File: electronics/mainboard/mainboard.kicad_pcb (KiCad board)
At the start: 2 copper layers, 43 x 137 mm, 20 parts, among them Q1 DMN2020LSN-7, SW1 SW_Push, SW10 SW_Push, SW11 SW_Push, SW12 SW_Push, SW13 SW_Push, SW14 SW_Push, SW15 SW_Push, SW2 SW_Push, SW3 SW_Push, SW4 SW_Push, SW5 SW_Push, SW6 SW_Push, SW7 SW_Push, SW8 SW_Push, SW9 SW_Push, U1 1022

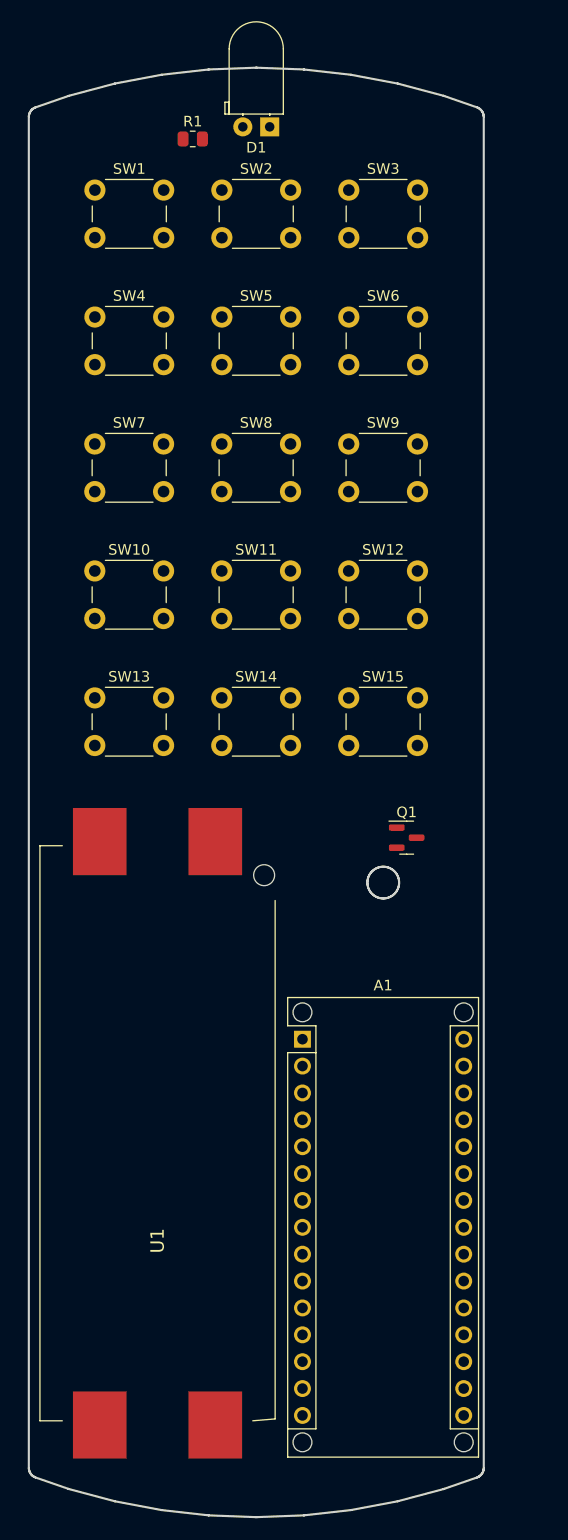
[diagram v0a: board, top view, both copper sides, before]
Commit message: modify closing mechanism and printing improvements - remove rounding (minkowski) for better printability - add closing mechanisms with levers   => remove backring as no longer needed   => remove positioning slits - correct case height to fit pcb - regenerate pcb outline and pcb 3d model because of some of the above changes
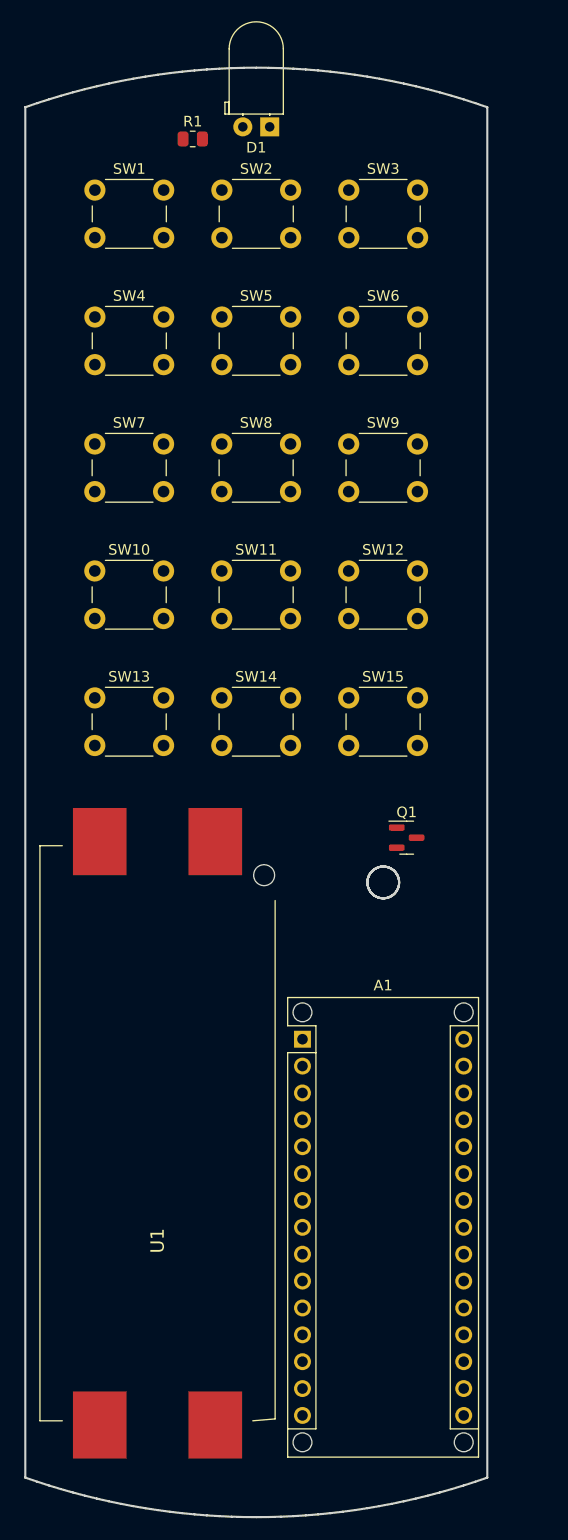
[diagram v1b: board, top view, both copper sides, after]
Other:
- board size 43 x 137 mm -> 43.7 x 137 mm

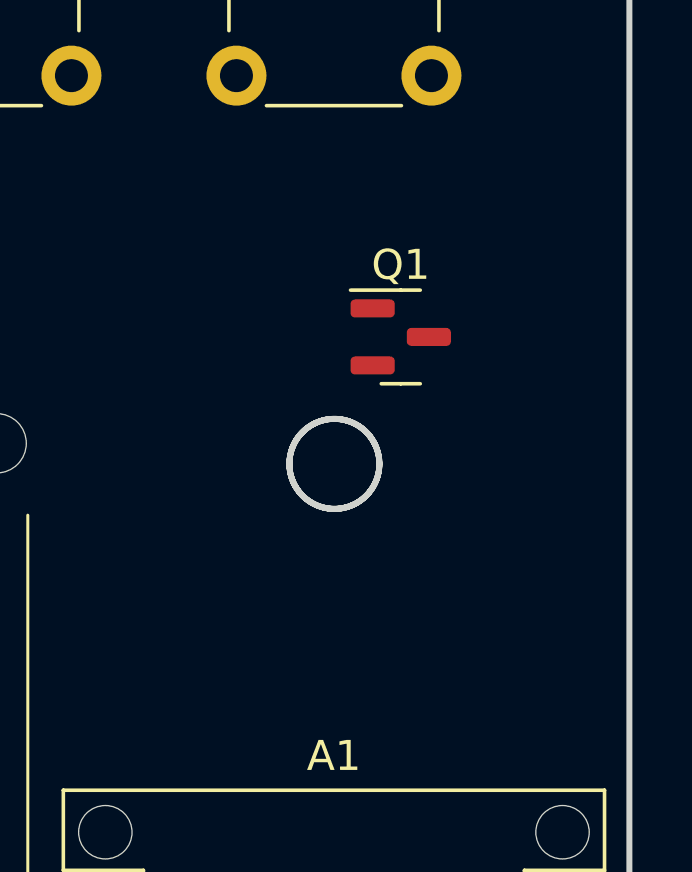
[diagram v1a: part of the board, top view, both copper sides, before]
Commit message: clean up libraries and  add more parts to desing - clean up libraries folder structure - no longer ignore important library table files - ignore auto save files - add fet for polarity protection - add buffer capacitors
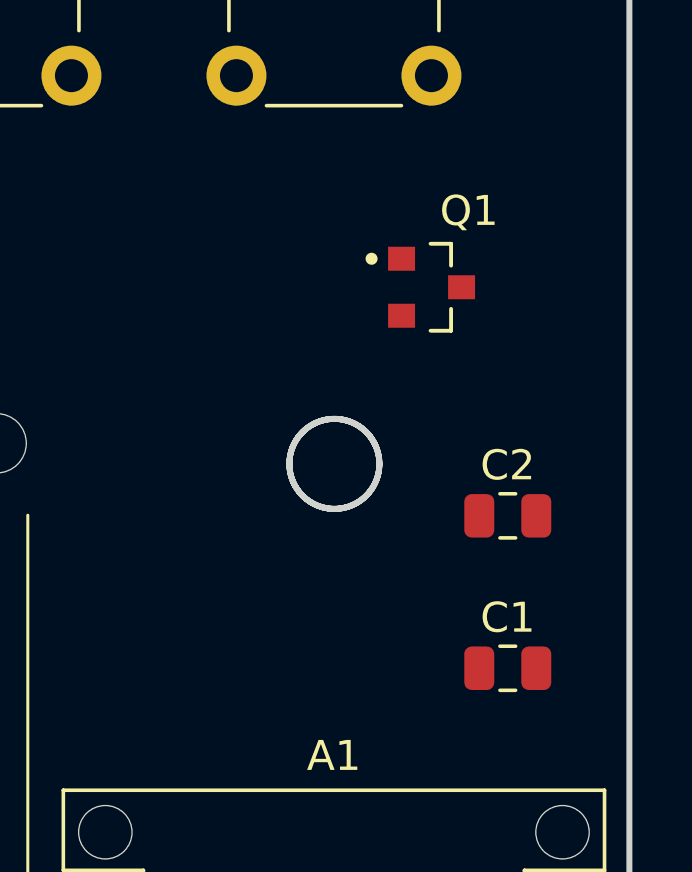
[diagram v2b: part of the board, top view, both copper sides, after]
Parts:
- added C1: 100u, Capacitor_SMD:C_0805_2012Metric, F.Cu at (128.0, 127.9)
- added C2: 100n, Capacitor_SMD:C_0805_2012Metric, F.Cu at (128.0, 122.8)
- Q1: value DMN2020LSN-7 -> TSM250N02CX_RFG; footprint Package_TO_SOT_SMD:SOT-23 -> TSM250N02CX_RFG:TRANS_TSM250N02CX_RFG
- moved Q1 1.95 mm to (125.5, 115.2)

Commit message: driver for ir-led and minor optimizations
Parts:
- added JP1: SolderJumper_2_Bridged, Jumper:SolderJumper-2_P1.3mm_Bridged_Pad1.0x1.5mm, F.Cu at (90.9, 110.1)
- added Q2: TSM250N02CX_RFG, TSM250N02CX_RFG:TRANS_TSM250N02CX_RFG, F.Cu at (120.4, 49.1)
- D1: value LED -> IR333-A
- R1: value R -> 82 1% 35mW
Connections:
- D1 pad 1: GND -> Net-(D1-Pad1)
- R1 pad 1: Net-(A1-Pad19) -> Net-(D1-Pad2)
- R1 pad 2: Net-(D1-Pad2) -> +3V0
- U1 pad 2: +3V0 -> Net-(U1-Pad2)
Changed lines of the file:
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@@
   (net 31 "Net-(A1-Pad19)")
   (net 32 "Net-(Q1-Pad3)")
+  (net 33 "Net-(D1-Pad1)")
+  (net 34 "Net-(U1-Pad2)")
+  (footprint "TSM250N02CX_RFG:TRANS_TSM250N02CX_RFG" (layer "F.Cu")
+    (at 120.4071 49.1437)
+    (property "MANUFACTURER" "Taiwan Semiconductor")
+    (property "MAXIMUM_PACKAGE_HEIGHT" "1.15mm")
+    (property "PARTREV" "A2007")
+    (property "STANDARD" "Manufacturer Recommendation")
+    (property "Sheetfile" "mainboard.kicad_sch")
+    (property "Sheetname" "")
+    (attr through_hole)
+    (fp_text reference "Q2" (at 1.25 -3.135) (layer "F.SilkS")
+      (effects (font (size 1 1) (thickness 0.15)))
+    )
+    (fp_text value "TSM250N02CX_RFG" (at 11.41 3.135) (layer "F.Fab")
+      (effects (font (size 1 1) (thickness 0.15)))
+    )
+    (fp_line (start -0.035 1.45) (end 0.65 1.45) (layer "F.SilkS") (width 0.127))
+    (fp_line (start 0.65 -1.45) (end -0.035 -1.45) (layer "F.SilkS") (width 0.127))
+    (fp_line (start 0.65 1.45) (end 0.65 0.72) (layer "F.SilkS") (width 0.127))
+    (fp_line (start 0.65 -0.72) (end 0.65 -1.45) (layer "F.SilkS") (width 0.127))
+    (fp_circle (center -2 -0.95) (end -1.9 -0.95) (layer "F.SilkS") (width 0.2) (fill none))
+    (fp_line (start -1.7 1.7) (end 1.7 1.7) (layer "F.CrtYd") (width 0.05))
+    (fp_line (start -1.7 -1.7) (end -1.7 1.7) (layer "F.CrtYd") (width 0.05))
+    (fp_line (start 1.7 1.7) (end 1.7 -1.7) (layer "F.CrtYd") (width 0.05))
+    (fp_line (start 1.7 -1.7) (end -1.7 -1.7) (layer "F.CrtYd") (width 0.05))
+    (fp_line (start -0.65 -1.45) (end -0.65 1.45) (layer "F.Fab") (width 0.127))
+    (fp_line (start -0.65 1.45) (end 0.65 1.45) (layer "F.Fab") (width 0.127))
+    (fp_line (start 0.65 -1.45) (end -0.65 -1.45) (layer "F.Fab") (width 0.127))
+    (fp_line (start 0.65 1.45) (end 0.65 -1.45) (layer "F.Fab") (width 0.127))
+    (fp_circle (center -2 -0.95) (end -1.9 -0.95) (layer "F.Fab") (width 0.2) (fill none))
+    (pad "1" smd rect locked (at -1 -0.95) (size 0.9 0.8) (layers "F.Cu" "F.Paste" "F.Mask")
+      (net 31 "Net-(A1-Pad19)") (pintype "passive"))
+    (pad "2" smd rect locked (at -1 0.95) (size 0.9 0.8) (layers "F.Cu" "F.Paste" "F.Mask")
+      (net 16 "GND") (pintype "passive"))
+    (pad "3" smd rect locked (at 1 0) (size 0.9 0.8) (layers "F.Cu" "F.Paste" "F.Mask")
+      (net 33 "Net-(D1-Pad1)") (pintype "passive"))
+    (model "${KIPRJMOD}/lib/TSM250N02CX_RFG/TSM250N02CX_RFG.step"
+      (offset (xyz 0 0 0))
+      (scale (xyz 1 1 1))
+      (rotate (xyz -90 0 0))
+    )
+  )
   (footprint "Capacitor_SMD:C_0805_2012Metric" (layer "F.Cu")
     (at 128.0271 122.8037)
@@
     (property "Sheetfile" "mainboard.kicad_sch")
     (property "Sheetname" "")
-    (property "exclude_from_bom" "")
-    (attr smd exclude_from_bom)
+    (attr smd)
     (fp_text reference "C2" (at 0 -1.68) (layer "F.SilkS")
       (effects (font (size 1 1) (thickness 0.15)))
@@
       (effects (font (size 1 1) (thickness 0.15)))
     )
-    (fp_text value "R" (at 0 1.65) (layer "F.Fab")
+    (fp_text value "82 1% 35mW" (at 0 1.65) (layer "F.Fab")
       (effects (font (size 1 1) (thickness 0.15)))
     )
@@
     (fp_line (start 1 -0.625) (end 1 0.625) (layer "F.Fab") (width 0.1))
     (pad "1" smd roundrect (at -0.9125 0) (size 1.025 1.4) (layers "F.Cu" "F.Paste" "F.Mask") (roundrect_rratio 0.243902)
-      (net 31 "Net-(A1-Pad19)") (pintype "passive"))
+      (net 12 "Net-(D1-Pad2)") (pintype "passive"))
     (pad "2" smd roundrect (at 0.9125 0) (size 1.025 1.4) (layers "F.Cu" "F.Paste" "F.Mask") (roundrect_rratio 0.243902)
-      (net 12 "Net-(D1-Pad2)") (pintype "passive"))
+      (net 17 "+3V0") (pintype "passive"))
     (model "${KICAD6_3DMODEL_DIR}/Resistor_SMD.3dshapes/R_0805_2012Metric.wrl"
       (offset (xyz 0 0 0))
@@
       (net 32 "Net-(Q1-Pad3)") (pinfunction "1") (pintype "passive"))
     (pad "2" smd rect (at -27.57 5.455) (size 5.08 6.35) (layers "F.Cu" "F.Paste" "F.Mask")
-      (net 17 "+3V0") (pinfunction "2") (pintype "passive"))
+      (net 34 "Net-(U1-Pad2)") (pinfunction "2") (pintype "passive"))
     (pad "3" smd rect (at 27.57 5.455) (size 5.08 6.35) (layers "F.Cu" "F.Paste" "F.Mask")
       (net 30 "Net-(U1-Pad3)") (pinfunction "3") (pintype "passive"))
@@
       (effects (font (size 1 1) (thickness 0.15)))
     )
-    (fp_text value "LED" (at 1.27 10.93) (layer "F.Fab")
+    (fp_text value "IR333-A" (at 1.27 10.93) (layer "F.Fab")
       (effects (font (size 1 1) (thickness 0.15)))
     )
@@
     (fp_arc (start 3.77 7.37) (mid 1.27 9.87) (end -1.23 7.37) (layer "F.Fab") (width 0.1))
     (pad "1" thru_hole rect (at 0 0 180) (size 1.8 1.8) (drill 0.9) (layers *.Cu *.Mask)
-      (net 16 "GND") (pinfunction "K") (pintype "passive"))
+      (net 33 "Net-(D1-Pad1)") (pinfunction "K") (pintype "passive"))
     (pad "2" thru_hole circle (at 2.54 0 180) (size 1.8 1.8) (drill 0.9) (layers *.Cu *.Mask)
       (net 12 "Net-(D1-Pad2)") (pinfunction "A") (pintype "passive"))
@@
     (property "Sheetfile" "mainboard.kicad_sch")
     (property "Sheetname" "")
-    (property "exclude_from_bom" "")
-    (attr smd exclude_from_bom)
+    (attr smd)
     (fp_text reference "C1" (at 0 -1.68) (layer "F.SilkS")
       (effects (font (size 1 1) (thickness 0.15)))
@@
     )
   )
+  (footprint "Jumper:SolderJumper-2_P1.3mm_Bridged_Pad1.0x1.5mm" (layer "F.Cu")
+    (at 90.857725 110.1037 90)
+    (descr "SMD Solder Jumper, 1x1.5mm Pads, 0.3mm gap, bridged with 1 copper strip")
+    (tags "net tie solder jumper bridged")
+    (property "Sheetfile" "mainboard.kicad_sch")
+    (property "Sheetname" "")
+    (attr exclude_from_pos_files)
+    (fp_text reference "JP1" (at 0 -1.8 90) (layer "F.SilkS")
+      (effects (font (size 1 1) (thickness 0.15)))
+    )
+    (fp_text value "SolderJumper_2_Bridged" (at 0 1.9 90) (layer "F.Fab")
+      (effects (font (size 1 1) (thickness 0.15)))
+    )
+    (fp_poly (pts
+        (xy -0.25 -0.3)
+        (xy 0.25 -0.3)
+        (xy 0.25 0.3)
+        (xy -0.25 0.3)
+      ) (layer "F.Cu") (width 0) (fill solid))
+    (fp_line (start 1.4 -1) (end 1.4 1) (layer "F.SilkS") (width 0.12))
+    (fp_line (start -1.4 -1) (end 1.4 -1) (layer "F.SilkS") (width 0.12))
+    (fp_line (start 1.4 1) (end -1.4 1) (layer "F.SilkS") (width 0.12))
+    (fp_line (start -1.4 1) (end -1.4 -1) (layer "F.SilkS") (width 0.12))
+    (fp_line (start 1.65 1.25) (end 1.65 -1.25) (layer "F.CrtYd") (width 0.05))
+    (fp_line (start 1.65 1.25) (end -1.65 1.25) (layer "F.CrtYd") (width 0.05))
+    (fp_line (start -1.65 -1.25) (end 1.65 -1.25) (layer "F.CrtYd") (width 0.05))
+    (fp_line (start -1.65 -1.25) (end -1.65 1.25) (layer "F.CrtYd") (width 0.05))
+    (pad "1" smd rect (at -0.65 0 90) (size 1 1.5) (layers "F.Cu" "F.Mask")
+      (net 34 "Net-(U1-Pad2)") (pinfunction "A") (pintype "passive"))
+    (pad "2" smd rect (at 0.65 0 90) (size 1 1.5) (layers "F.Cu" "F.Mask")
+      (net 17 "+3V0") (pinfunction "B") (pintype "passive"))
+  )
   (footprint "Module:Arduino_Nano_WithMountingHoles" (layer "F.Cu")

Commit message: route pcb
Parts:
- moved Q2 80.6 mm to (129.9, 129.2), turned to 90 degrees
- moved C2 43.3 mm to (90.9, 100.6)
- moved C1 42.6 mm to (90.9, 106.9)
- moved Q1 17.7 mm to (114.7, 129.2), turned to 90 degrees
- moved R1 3.68 mm to (100.8, 49.6), turned to 180 degrees
- moved JP1 1.56 mm to (89.9, 111.4)
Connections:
- A1 pad 1: /SW2 -> /SW13
- A1 pad 11: /SW9 -> /SW5
- A1 pad 12: /SW10 -> /SW2
- A1 pad 13: /SW11 -> /SW15
- A1 pad 15: /SW13 -> /SW9
- A1 pad 16: /SW14 -> unconnected-(A1-Pad16)
- A1 pad 19: Net-(A1-Pad19) -> unconnected-(A1-Pad19)
- A1 pad 2: /SW1 -> /SW10
- A1 pad 24: unconnected-(A1-Pad24) -> /SW6
- A1 pad 25: unconnected-(A1-Pad25) -> /SW3
- A1 pad 26: /SW15 -> Net-(A1-Pad26)
- A1 pad 5: /SW3 -> /SW7
- A1 pad 7: /SW5 -> /SW1
- A1 pad 8: /SW6 -> /SW14
- A1 pad 9: /SW7 -> /SW11
- Q2 pad 1: Net-(A1-Pad19) -> Net-(A1-Pad26)
- SW10 pad 2: /SW12 -> /SW10
- SW12 pad 2: /SW10 -> /SW12
- SW13 pad 2: /SW15 -> /SW13
- SW15 pad 2: /SW13 -> /SW15
- SW2 pad 2: /SW3 -> /SW2
- SW3 pad 2: /SW2 -> /SW3
- SW4 pad 2: /SW6 -> /SW4
- SW6 pad 2: /SW4 -> /SW6
- SW7 pad 2: /SW9 -> /SW7
- SW9 pad 2: /SW7 -> /SW9
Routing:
- net /SW2: track 0.00 -> 119.1 mm
- net /SW1: track 0.00 -> 112.1 mm
- net /SW5: track 0.00 -> 104.1 mm
- net /SW9: track 0.00 -> 100.4 mm
- net /SW3: track 0.00 -> 97.8 mm
- net /SW4: track 0.00 -> 97.1 mm
- net Net-(D1-Pad1): track 0.00 -> 94.4 mm
- net /SW8: track 0.00 -> 89.0 mm
- net /SW6: track 0.00 -> 88.4 mm
- net /SW12: track 0.00 -> 85.4 mm
- net /SW7: track 0.00 -> 82.0 mm
- net /SW11: track 0.00 -> 74.0 mm
- net /SW15: track 0.00 -> 69.2 mm
- net /SW10: track 0.00 -> 61.9 mm
- net /SW14: track 0.00 -> 58.9 mm
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- added copper zone on F.Cu, net +3V0
- added copper zone on B.Cu, net GND
- added copper zone on F.Cu, net GND

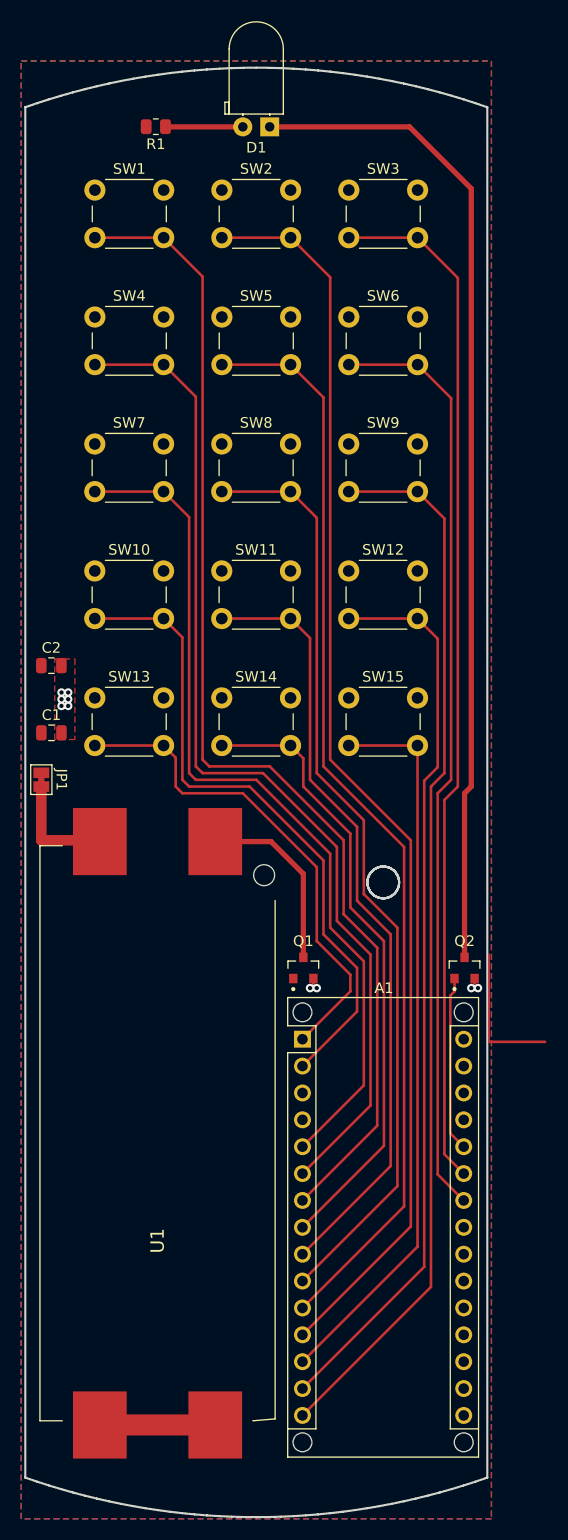
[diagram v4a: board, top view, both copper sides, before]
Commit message: resolve drc errors and warnings
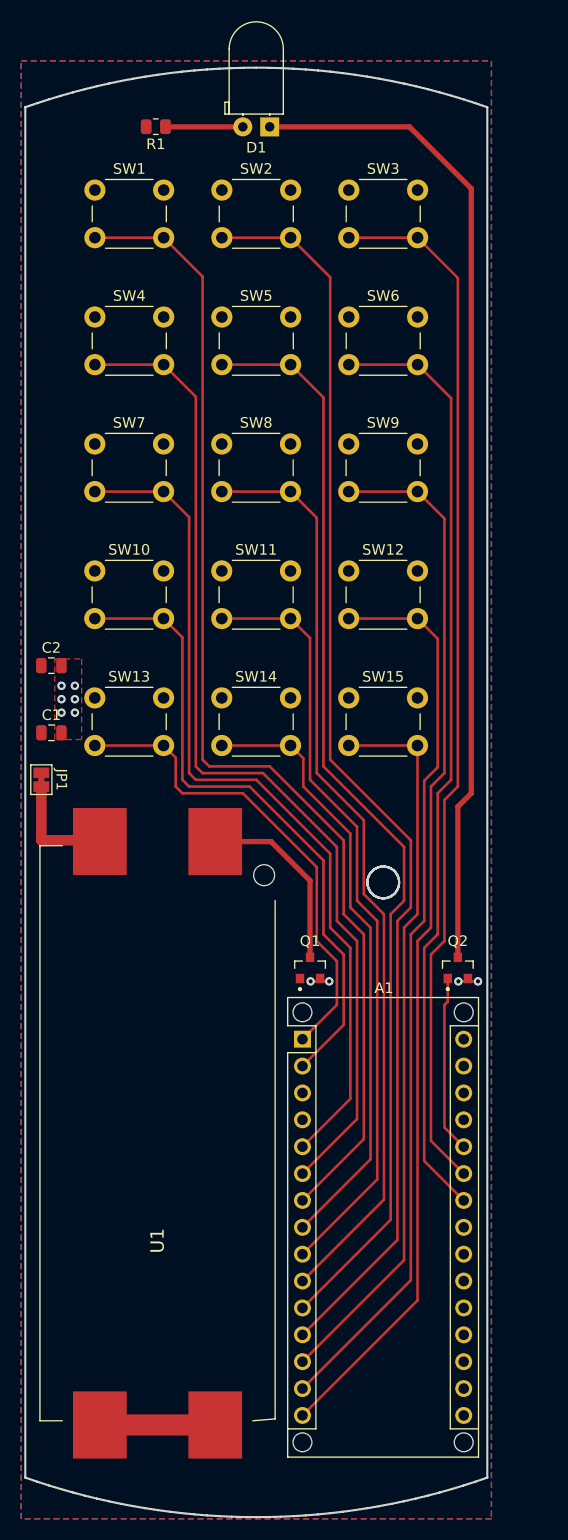
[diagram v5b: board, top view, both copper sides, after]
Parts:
- moved Q1 0.64 mm to (115.3, 129.2)
- moved Q2 0.63 mm to (129.3, 129.2)
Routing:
- net (no net): track 13.6 -> 0.00 mm
- net GND: track 5.42 -> 4.07 mm
- net /SW6: track 88.4 -> 89.4 mm
- net /SW13: track 46.8 -> 45.7 mm
- net /SW10: track 61.9 -> 60.8 mm
- net /SW4: track 97.1 -> 96.0 mm
- net /SW3: track 97.8 -> 98.9 mm
- net /SW11: track 74.0 -> 72.9 mm
- net /SW14: track 58.9 -> 57.8 mm
- net /SW8: track 89.0 -> 88.0 mm
- net /SW7: track 82.0 -> 81.0 mm
- net /SW1: track 112.1 -> 111.1 mm

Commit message: clarify designator of arduino
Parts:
- A1: value Arduino_Nano_v3.x -> Arduino_Nano_33_BLE
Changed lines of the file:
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@@
       (effects (font (size 1 1) (thickness 0.15)))
     )
-    (fp_text value "Arduino_Nano_v3.x" (at 8.89 15.24 90) (layer "F.Fab")
+    (fp_text value "Arduino_Nano_33_BLE" (at 8.89 15.24 90) (layer "F.Fab")
       (effects (font (size 1 1) (thickness 0.15)))
     )
